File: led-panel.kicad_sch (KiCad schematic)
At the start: 12 parts

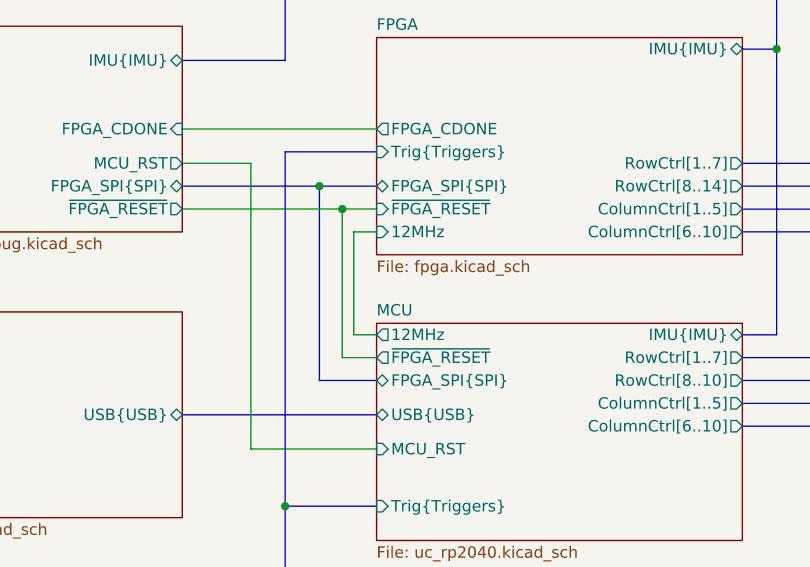
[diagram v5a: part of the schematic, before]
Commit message: [#72447] Update clock & SPI connections
Signed-off-by: Dawid Lentka <dlentka@antmicro.com>
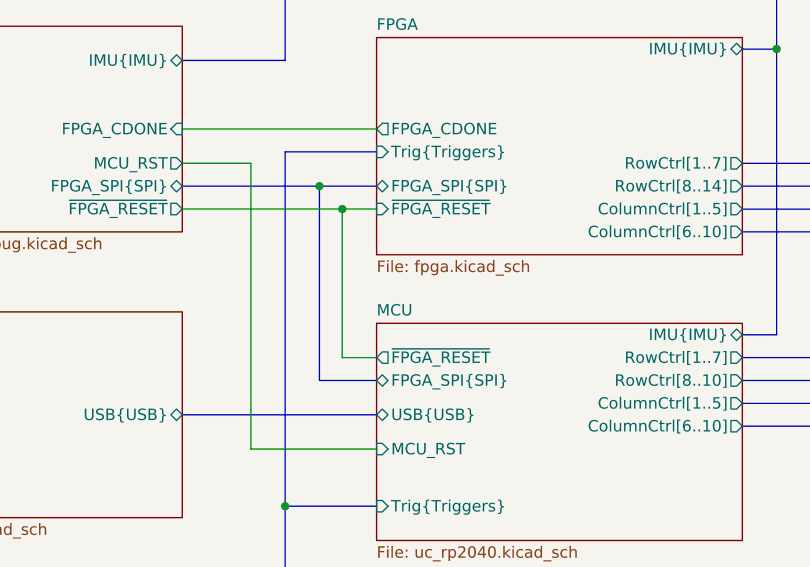
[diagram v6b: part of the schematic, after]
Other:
- sheet FPGA ports: added none; removed 12MHz
- sheet MCU ports: added none; removed 12MHz
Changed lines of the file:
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@@
 		(color 0 0 0 0)
 	)
-	(wire
-		(pts
-			(xy 88.9 87.63) (xy 88.9 99.06)
-		)
-		(stroke
-			(width 0)
-			(type default)
-		)
-	)
 	(bus
 		(pts
@@
 		)
 	)
-	(wire
-		(pts
-			(xy 88.9 99.06) (xy 91.44 99.06)
-		)
-		(stroke
-			(width 0)
-			(type default)
-		)
-	)
 	(bus
 		(pts
@@
 		(pts
 			(xy 69.85 107.95) (xy 91.44 107.95)
-		)
-		(stroke
-			(width 0)
-			(type default)
-		)
-	)
-	(wire
-		(pts
-			(xy 88.9 87.63) (xy 91.44 87.63)
 		)
 		(stroke
@@
 			)
 		)
-		(pin "12MHz" output
-			(at 91.44 99.06 180)
-			(effects
-				(font
-					(size 1.27 1.27)
-				)
-				(justify left)
-			)
-		)
 		(pin "RowCtrl[1..7]" output
 			(at 132.08 101.6 0)
@@
 			(effects
 				(font
-					(size 1.27 1.27)
-				)
-				(justify left)
-			)
-		)
-		(pin "12MHz" input
-			(at 91.44 87.63 180)
-			(effects
-				(font

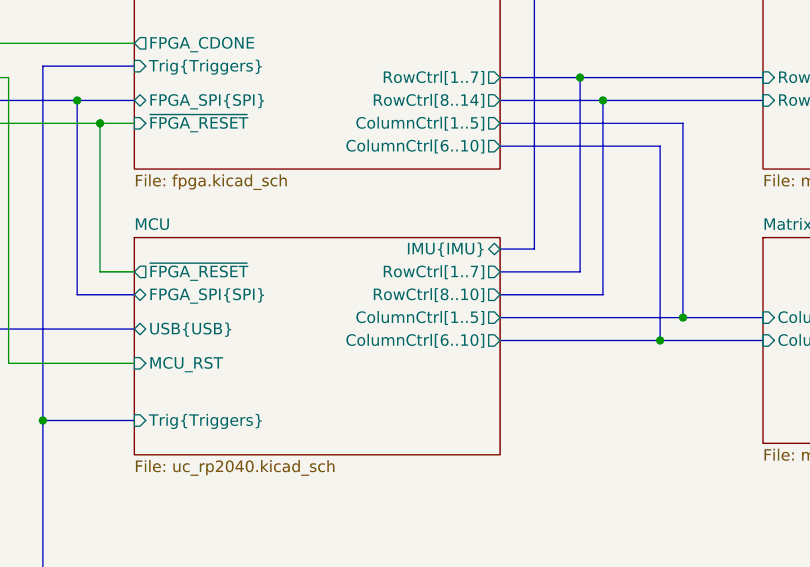
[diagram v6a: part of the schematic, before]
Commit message: [#72447] SCH: Update matrix drive resistors
Signed-off-by: Dawid Lentka <dlentka@antmicro.com>
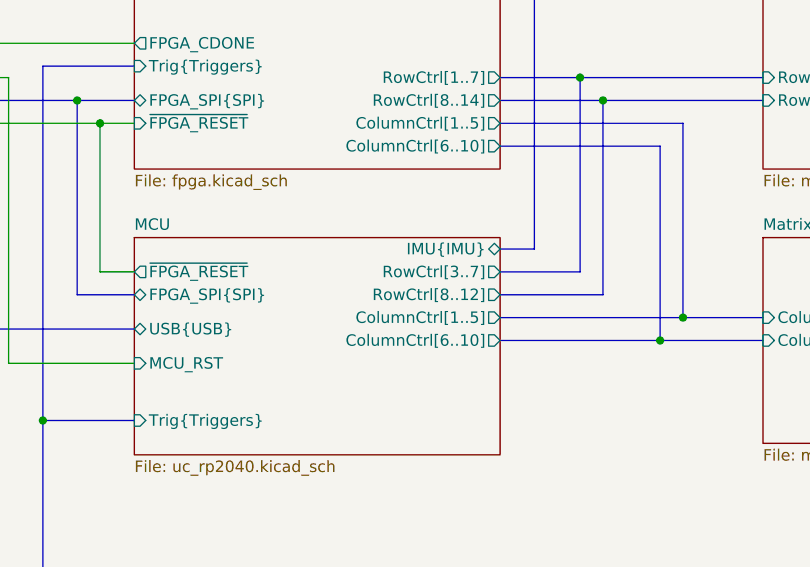
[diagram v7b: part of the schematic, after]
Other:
- sheet MCU ports: added RowCtrl[3..7], RowCtrl[8..12]; removed RowCtrl[1..7], RowCtrl[8..10]
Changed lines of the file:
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@@
 	(title_block
 		(title "LED Panel Board")
-		(date "2025-01-31")
+		(date "2025-02-04")
 		(rev "1.0.0")
 	)
@@
 			)
 		)
-		(pin "RowCtrl[1..7]" output
+		(pin "RowCtrl[3..7]" output
 			(at 132.08 101.6 0)
 			(effects
@@
 			)
 		)
-		(pin "RowCtrl[8..10]" output
+		(pin "RowCtrl[8..12]" output
 			(at 132.08 104.14 0)
 			(effects
